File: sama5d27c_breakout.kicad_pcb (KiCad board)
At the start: 4 copper layers, 234 parts, among them J1 Conn_LCD, J10 Conn_Speaker, J2 Conn_JTAG, J3 Conn_SDMMC0, J4 Conn_FLEXCOM3_4, J5 Conn_DBGU, J6 Conn_BAT, J7 USB_C_Receptacle_USB2.0, J8 USB_B_Micro, J9 Micro_SD_Card_Det, Q1 BSS138, Q2 BSS138, Q3 BSS138, Q4 BSS138, Q5 BSS138, Q6 BSS138, Q7 BSS138, Q8 BSS138, SW1 SW_WAKEUP, SW2 SW_RESET, SW3 SW_USR, U1 SAMA5D2x-SIP, U2 ACT8945A, U3 MIC2025, U4 IS25LP128F, U5 DMC2450, U6 DMC2450, Y1 TSX-3225 24MHz, Y2 32kHz

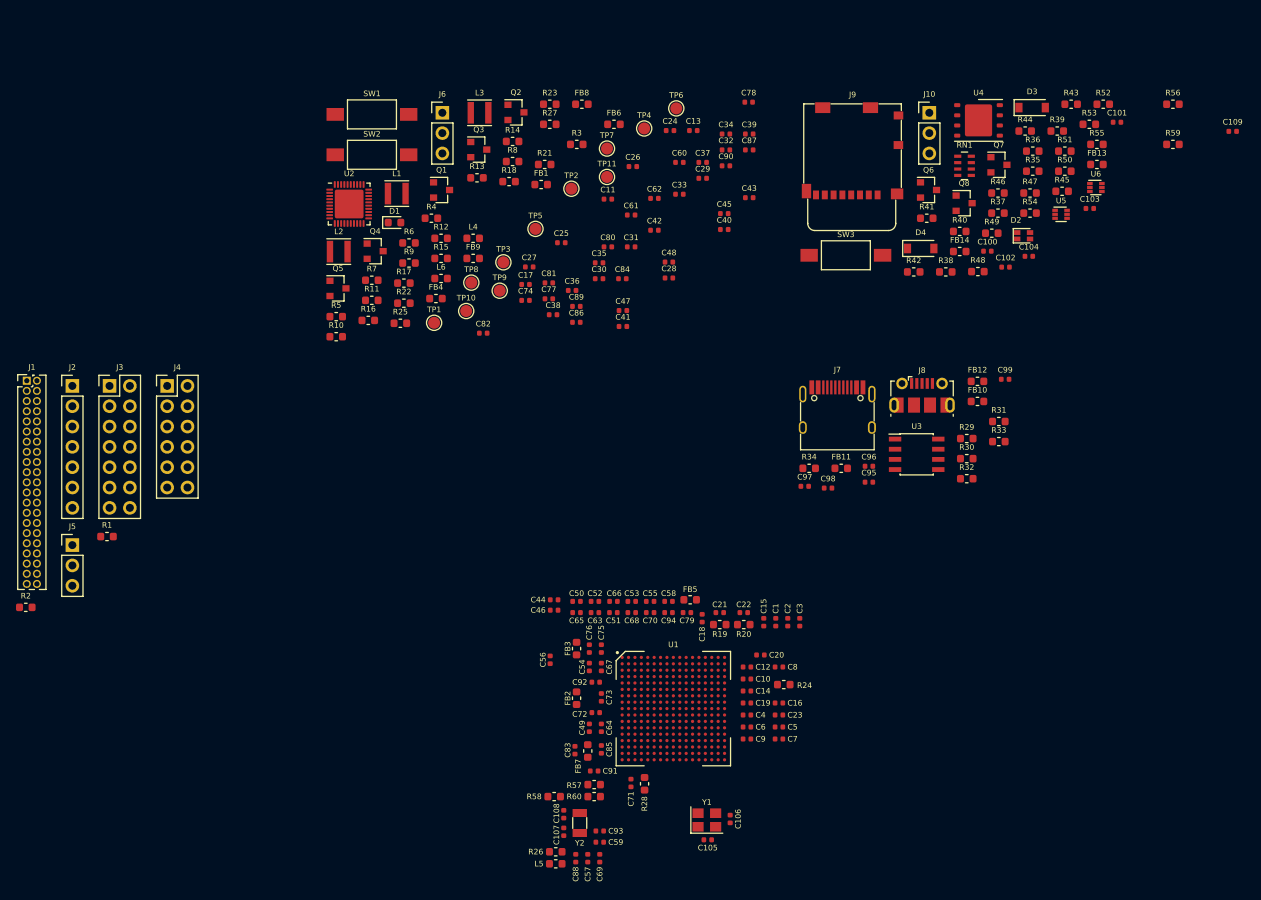
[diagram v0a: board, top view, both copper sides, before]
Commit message: Start the routing
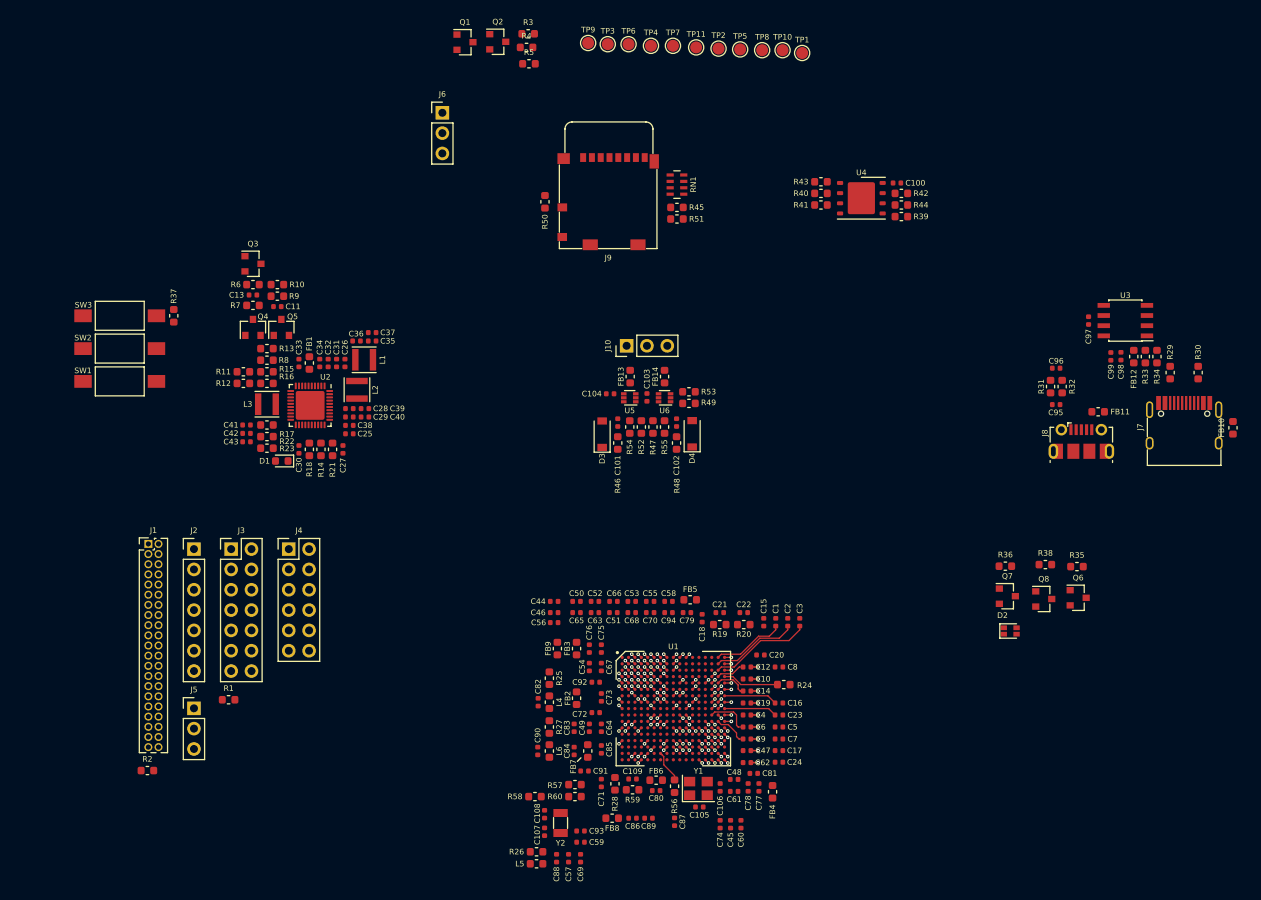
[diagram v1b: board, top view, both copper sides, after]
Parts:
- moved C109 110.4 mm to (159.4, 139.5)
- moved R56 105.6 mm to (164.7, 140.4), turned to 270 degrees
- moved R59 105.2 mm to (159.4, 140.8)
- moved R37 103.8 mm to (102.0, 81.6), turned to 270 degrees
- moved SW3 91.1 mm to (95.3, 81.6), turned to 180 degrees
- moved FB8 89.3 mm to (156.8, 144.4)
- moved C78 85.7 mm to (173.8, 140.6), turned to 270 degrees
- moved C87 84.5 mm to (164.7, 144.8), turned to 270 degrees
- moved C60 83.1 mm to (172.9, 145.2), turned to 90 degrees
- moved FB6 82.2 mm to (162.3, 139.7)
- moved C24 80.1 mm to (177.7, 137.4), turned to 180 degrees
- moved C90 76.8 mm to (147.6, 136.0), turned to 90 degrees
- moved C45 76.3 mm to (171.7, 145.2), turned to 90 degrees
- moved R27 75.3 mm to (149.0, 133.0), turned to 90 degrees
- moved FB4 74.6 mm to (176.9, 141.1), turned to 90 degrees
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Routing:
- net +1V35: track 0.00 -> 67.7 mm, vias 0 -> 7
- net GND: track 0.00 -> 34.8 mm, vias 0 -> 52
- net Net-(R24-Pad2): track 0.00 -> 7.03 mm
- net Net-(R56-Pad1): track 0.00 -> 4.04 mm
- net Net-(C75-Pad1): track 0.00 -> 1.13 mm, vias 0 -> 2
- net /SDMMC1_DAT2: track 0.00 -> 0.61 mm, vias 0 -> 1
- net /LCD_DAT10: track 0.00 -> 0.61 mm, vias 0 -> 1
- net Net-(C82-Pad1): track 0.00 -> 0.57 mm, vias 0 -> 1
- net /USR_BTN: track 0.00 -> 0.57 mm, vias 0 -> 1
- net /SPI0_SPCK: track 0.00 -> 0.57 mm, vias 0 -> 1
- net /SPI0_NPCS0: track 0.00 -> 0.57 mm, vias 0 -> 1
- net /SPI0_MOSI: track 0.00 -> 0.57 mm, vias 0 -> 1
- net /SPI0_MISO: track 0.00 -> 0.57 mm, vias 0 -> 1
- net /SDMMC1_CDA: track 0.00 -> 0.57 mm, vias 0 -> 1
- net /SDMMC1_CD: track 0.00 -> 0.57 mm, vias 0 -> 1
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- added copper zone on In1.Cu.GND, net GND
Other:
- net class Power added: clearance 0.1, trace_width 0.2, via_dia 0.45, via_drill 0.2
- board text added: "Change 10uF to 0603?"
- board text added: "Flip!"
- board text added: "Remove MOSFETs"

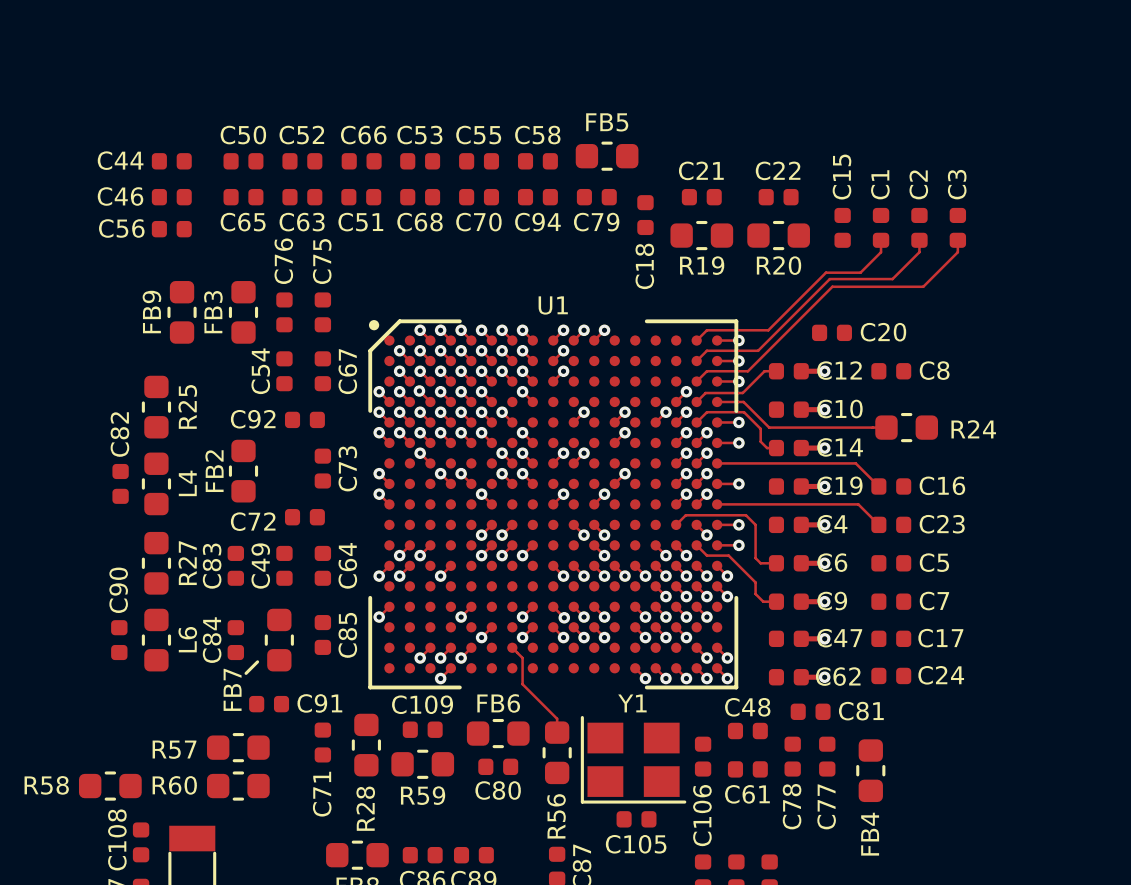
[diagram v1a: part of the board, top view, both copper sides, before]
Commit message: Route more power traces
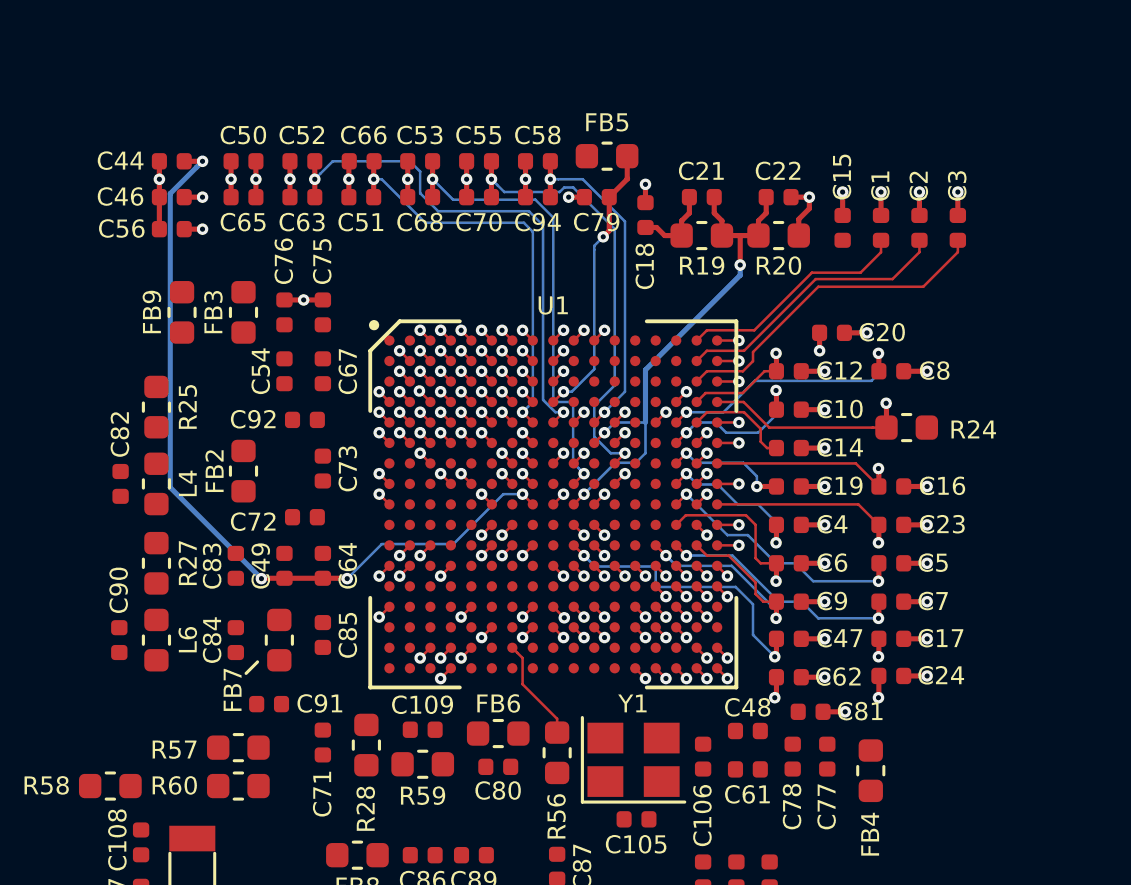
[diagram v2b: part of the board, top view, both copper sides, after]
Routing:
- net +1V35: track 67.7 -> 235.4 mm, vias 7 -> 36
- net GND: track 34.8 -> 62.9 mm, vias 52 -> 76
- net +1V2: track 0.00 -> 23.2 mm, vias 0 -> 5
- net Net-(C21-Pad1): track 0.00 -> 20.7 mm, vias 0 -> 3
- net Net-(C79-Pad1): track 0.00 -> 11.0 mm, vias 0 -> 2
- net Net-(R24-Pad2): track 7.03 -> 7.98 mm, vias 0 -> 1
- net +3V3: track 0.00 -> 0.72 mm, vias 0 -> 1
- added copper zone on In2.Cu.VDD, net +1V35

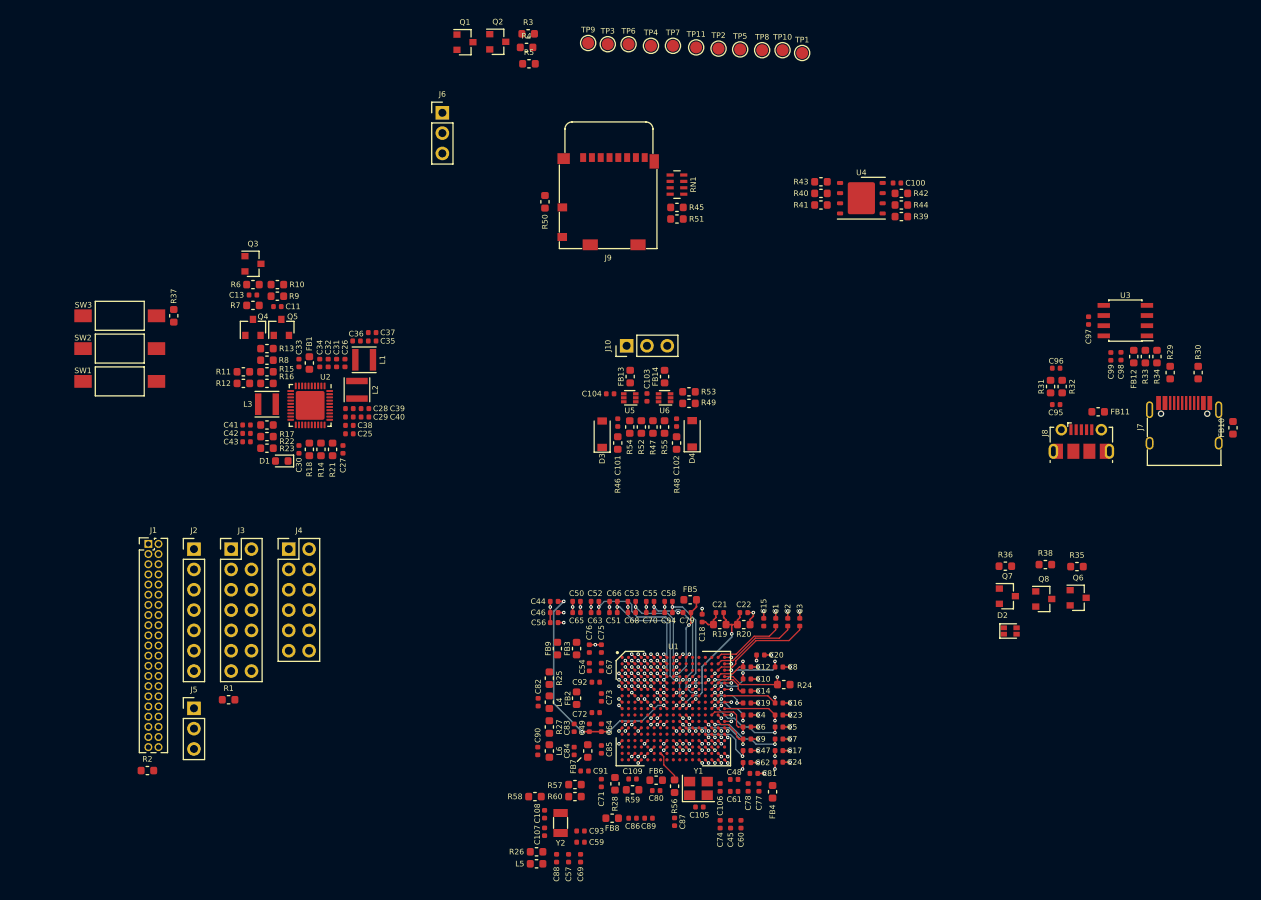
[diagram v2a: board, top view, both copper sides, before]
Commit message: More routing, 165 unconnected left
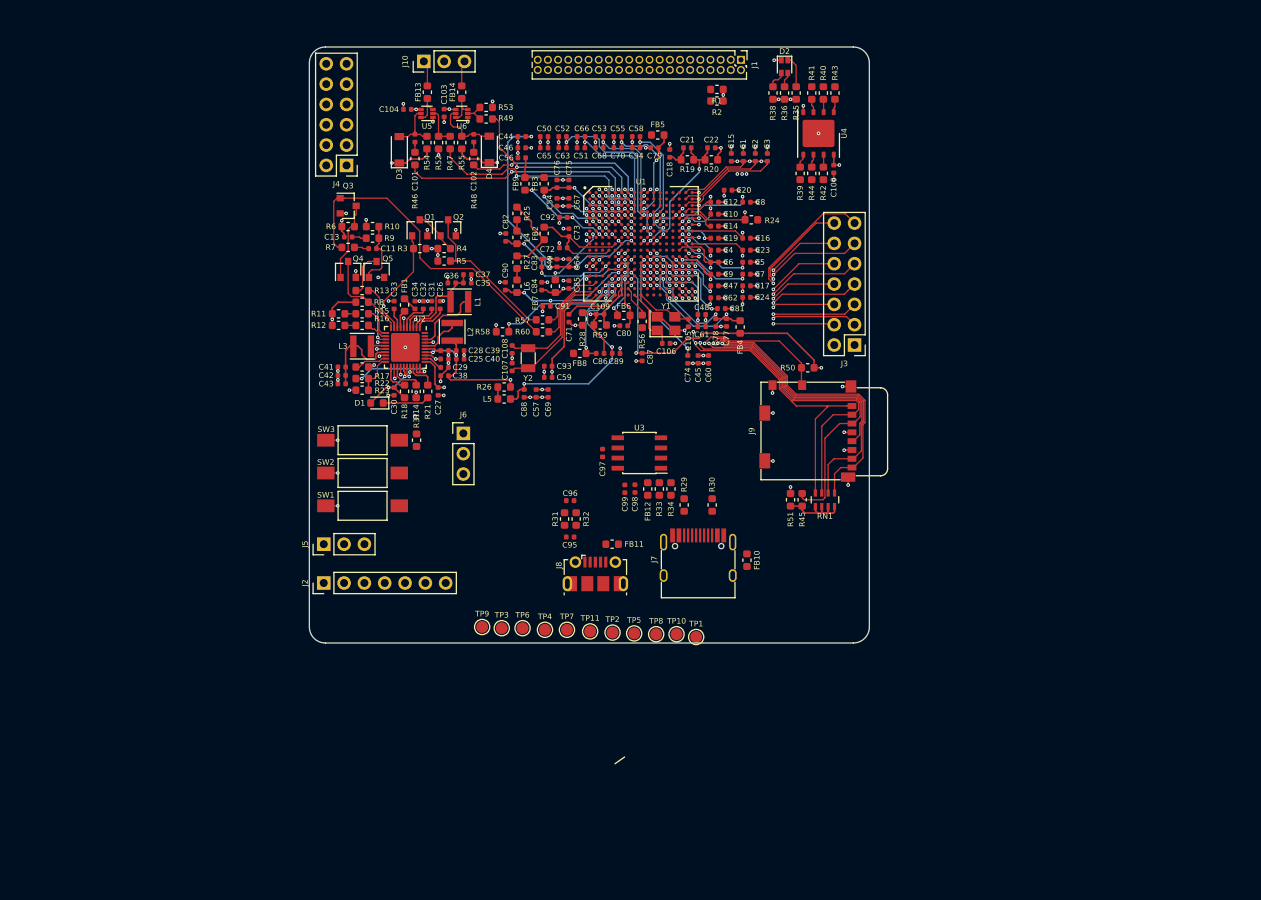
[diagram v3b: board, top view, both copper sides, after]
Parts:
- removed Q6, Q7, Q8: BSS138, Package_TO_SOT_SMD:SOT-23
- moved R2 109.9 mm to (169.9, 54.8), turned to 180 degrees
- moved R1 97.7 mm to (169.9, 53.3), turned to 180 degrees
- moved J1 95.7 mm to (172.9, 49.6), turned to 270 degrees
- moved J3 82.0 mm to (187.2, 85.2), turned to 180 degrees
- moved D2 76.0 mm to (178.4, 50.5), turned to 270 degrees
- moved TP1 74.2 mm to (167.3, 121.8)
- moved TP10 74.2 mm to (164.9, 121.4)
- moved TP11 74.2 mm to (154.1, 121.0)
- moved TP2 74.2 mm to (156.9, 121.2)
- moved TP3 74.2 mm to (143.1, 120.7)
- moved TP4 74.2 mm to (148.4, 120.8)
- moved TP5 74.2 mm to (159.6, 121.3)
- moved TP6 74.2 mm to (145.7, 120.7)
- moved TP7 74.2 mm to (151.2, 120.8)
- moved TP8 74.2 mm to (162.3, 121.4)
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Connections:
- D2 pad 2: Net-(D2-Pad2) -> /LED_RED
- D2 pad 3: Net-(D2-Pad3) -> /LED_GREEN
- D2 pad 4: Net-(D2-Pad4) -> /LED_BLUE
- R35 pad 1: GND -> /LED_RED
- R35 pad 2: /LED_RED -> +3V3
- R36 pad 1: GND -> /LED_GREEN
- R36 pad 2: /LED_GREEN -> +3V3
- R38 pad 1: GND -> /LED_BLUE
- R38 pad 2: /LED_BLUE -> +3V3
- R50 pad 2: Net-(R45-Pad2) -> +3V3
- RN1 pad 1: /SDMMC1_DAT2 -> /SDMMC1_DAT1
- RN1 pad 2: /SDMMC1_DAT3 -> /SDMMC1_DAT0
- RN1 pad 3: /SDMMC1_DAT0 -> /SDMMC1_DAT3
- RN1 pad 4: /SDMMC1_DAT1 -> /SDMMC1_DAT2
- Y1 pad 1: Net-(C105-Pad1) -> Net-(C106-Pad1)
- Y1 pad 3: Net-(C106-Pad1) -> Net-(C105-Pad1)
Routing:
- net GND: track 62.9 -> 135.2 mm, vias 76 -> 148
- net +1V2: track 23.2 -> 95.3 mm, vias 5 -> 17
- net +3V3: track 0.72 -> 69.5 mm, vias 1 -> 10
- net /SDMMC1_CDA: track 0.57 -> 51.3 mm, vias 1 -> 2
- net /SDMMC1_DAT3: track 0.57 -> 51.3 mm, vias 1 -> 2
- net /SDMMC1_DAT2: track 0.61 -> 48.1 mm, vias 1 -> 3
- net /SDMMC1_DAT1: track 0.00 -> 46.2 mm, vias 0 -> 2
- net +5V: track 0.00 -> 45.7 mm, vias 0 -> 13
- net /SDMMC1_DAT0: track 0.57 -> 45.6 mm, vias 1 -> 2
- net /SHDN: track 0.00 -> 40.8 mm
- net /SDMMC1_CK: track 0.57 -> 35.1 mm, vias 1 -> 2
- net VDDA: track 0.00 -> 32.4 mm, vias 0 -> 2
- net /CLASSD_R0: track 0.57 -> 32.1 mm, vias 1 -> 2
- net /SDMMC0_CDA: track 0.00 -> 30.1 mm, vias 0 -> 2
- net Net-(C88-Pad1): track 0.00 -> 29.9 mm, vias 0 -> 3
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- added copper zone on In2.Cu.VDD, net +1V2
- added copper zone on In2.Cu.VDD, net +3V3
- added copper zone on In2.Cu.VDD, net +5V
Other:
- board outline added: 70 x 74.5 mm
- board text removed: "Change 10uF to 0603?"
- board text removed: "Flip!"
- board text removed: "Remove MOSFETs"

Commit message: Fix USB bug by updating symbols lib
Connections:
- FB10 pad 1: GND -> Net-(FB10-Pad1)
- FB12 pad 1: VBUS -> /USB/B_VBUS
- J7 pad A1: GND -> Net-(FB10-Pad1)
- J7 pad A12: GND -> Net-(FB10-Pad1)
- J7 pad A4: VBUS -> /USB/B_VBUS
- J7 pad A9: VBUS -> /USB/B_VBUS
- J7 pad B1: GND -> Net-(FB10-Pad1)
- J7 pad B12: GND -> Net-(FB10-Pad1)
- J7 pad B4: VBUS -> /USB/B_VBUS
- J7 pad B9: VBUS -> /USB/B_VBUS
- J7 pad S1: GND -> Net-(FB10-Pad1)
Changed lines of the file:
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@@
-(kicad_pcb (version 20171130) (host pcbnew "(6.0.0-rc1-dev-1009-g96e65c7f2)")
+(kicad_pcb (version 20171130) (host pcbnew "(6.0.0-rc1-dev-1050-geabae68ab)")
   (general
     (thickness 1.6)
@@
     (zones 0)
     (modules 231)
-    (nets 278)
+    (nets 280)
   )
   (page A4)
@@
   (net 276 /PMIC_TWCK)
   (net 277 /PMIC_TWD)
+  (net 278 "Net-(FB10-Pad1)")
+  (net 279 /USB/B_VBUS)
   (net_class Default "This is the default net class."
     (clearance 0.1)
@@
     (add_net "Net-(D1-Pad1)")
     (add_net "Net-(FB1-Pad1)")
+    (add_net "Net-(FB10-Pad1)")
     (add_net "Net-(FB11-Pad1)")
     (add_net "Net-(FB13-Pad1)")
@@
     (add_net /Power/VDDSDHC1V8)
     (add_net /Power/VDD_LED)
+    (add_net /USB/B_VBUS)
     (add_net GND)
     (add_net GNDS)
@@
     (fp_line (start -4.97 5.15) (end 5.1 5.15) (layer F.CrtYd) (width 0.12))
     (pad S1 thru_hole oval (at -4.32 1.87) (size 1 1.6) (drill oval 0.6 1.2) (layers *.Cu *.Mask)
-      (net 2 GND))
+      (net 278 "Net-(FB10-Pad1)"))
     (pad S1 thru_hole oval (at 4.32 1.87) (size 1 1.6) (drill oval 0.6 1.2) (layers *.Cu *.Mask)
-      (net 2 GND))
+      (net 278 "Net-(FB10-Pad1)"))
     (pad S1 thru_hole oval (at -4.32 -2.31) (size 0.9 2.1) (drill oval 0.5 1.7) (layers *.Cu *.Mask)
-      (net 2 GND))
+      (net 278 "Net-(FB10-Pad1)"))
     (pad S1 thru_hole oval (at 4.32 -2.31) (size 0.9 2.1) (drill oval 0.5 1.7) (layers *.Cu *.Mask)
-      (net 2 GND))
+      (net 278 "Net-(FB10-Pad1)"))
     (pad "" np_thru_hole circle (at -2.89 -1.81) (size 0.65 0.65) (drill 0.65) (layers *.Cu *.Mask))
     (pad "" np_thru_hole circle (at 2.89 -1.81) (size 0.65 0.65) (drill 0.65) (layers *.Cu *.Mask))
@@
       (net 202 /USB/B_D+))
     (pad A1 smd rect (at -3.35 -3.15) (size 0.3 1.75) (layers F.Cu F.Paste F.Mask)
-      (net 2 GND))
+      (net 278 "Net-(FB10-Pad1)"))
     (pad B12 smd rect (at -3.05 -3.15) (size 0.3 1.75) (layers F.Cu F.Paste F.Mask)
-      (net 2 GND))
+      (net 278 "Net-(FB10-Pad1)"))
     (pad A4 smd rect (at -2.55 -3.15) (size 0.3 1.75) (layers F.Cu F.Paste F.Mask)
-      (net 99 VBUS))
+      (net 279 /USB/B_VBUS))
     (pad B9 smd rect (at -2.25 -3.15) (size 0.3 1.75) (layers F.Cu F.Paste F.Mask)
-      (net 99 VBUS))
+      (net 279 /USB/B_VBUS))
     (pad A9 smd rect (at 2.55 -3.15) (size 0.3 1.75) (layers F.Cu F.Paste F.Mask)
-      (net 99 VBUS))
+      (net 279 /USB/B_VBUS))
     (pad B4 smd rect (at 2.25 -3.15) (size 0.3 1.75) (layers F.Cu F.Paste F.Mask)
-      (net 99 VBUS))
+      (net 279 /USB/B_VBUS))
     (pad B1 smd rect (at 3.05 -3.15) (size 0.3 1.75) (layers F.Cu F.Paste F.Mask)
-      (net 2 GND))
+      (net 278 "Net-(FB10-Pad1)"))
     (pad A12 smd rect (at 3.35 -3.15) (size 0.3 1.75) (layers F.Cu F.Paste F.Mask)
-      (net 2 GND))
+      (net 278 "Net-(FB10-Pad1)"))
     (model ${KIPRJMOD}/modules/packages3d/Connector_USB.3dshapes/KUSBX-SMT-CS2-BTR_rA1.STEP
       (offset (xyz 0 -4.7 1.6))
@@
       (net 117 "Net-(C98-Pad2)"))
     (pad 1 smd roundrect (at -0.7875 0 90) (size 0.875 0.95) (layers F.Cu F.Paste F.Mask) (roundrect_rratio 0.25)
-      (net 99 VBUS))
+      (net 279 /USB/B_VBUS))
     (model ${KISYS3DMOD}/Inductor_SMD.3dshapes/L_0603_1608Metric.wrl
       (at (xyz 0 0 0))
@@
     )
     (pad 1 smd roundrect (at -0.7875 0 90) (size 0.875 0.95) (layers F.Cu F.Paste F.Mask) (roundrect_rratio 0.25)
-      (net 2 GND))
+      (net 278 "Net-(FB10-Pad1)"))
     (pad 2 smd roundrect (at 0.7875 0 90) (size 0.875 0.95) (layers F.Cu F.Paste F.Mask) (roundrect_rratio 0.25)
       (net 2 GND))
